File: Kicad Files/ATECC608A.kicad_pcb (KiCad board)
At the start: 2 copper layers, 26.7 x 22.8 mm, 12 parts, among them J1 Conn_01x04, U1 ATECC608A-SSHDA

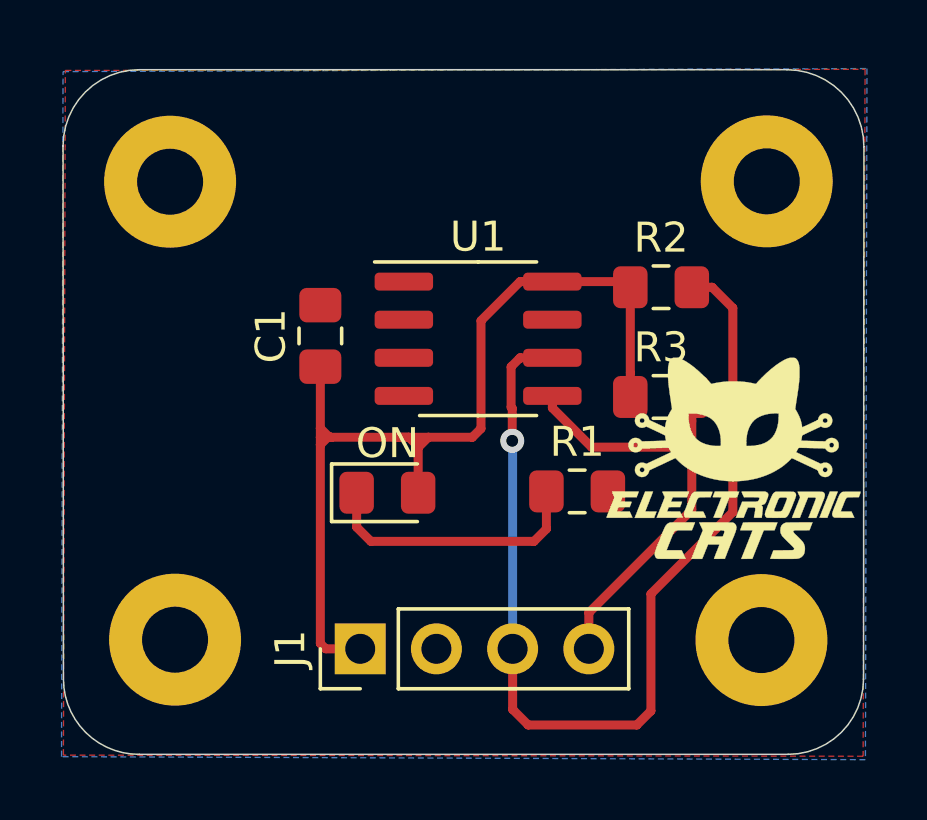
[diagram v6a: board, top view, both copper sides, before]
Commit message: add logos
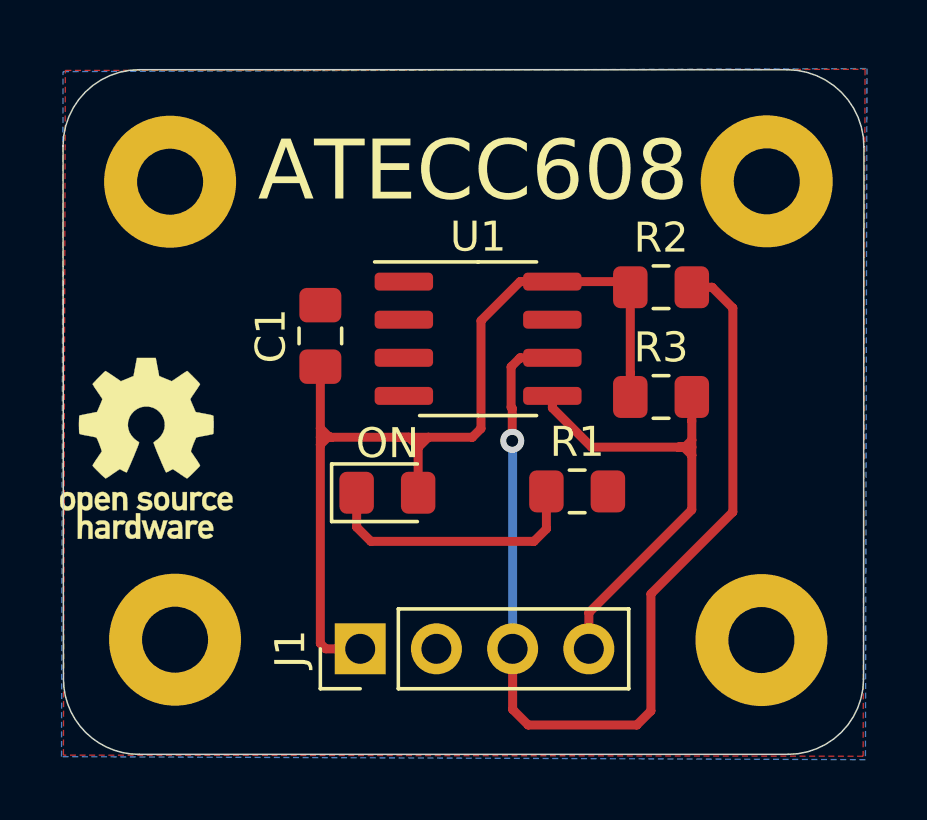
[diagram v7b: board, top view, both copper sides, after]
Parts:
- added REF**: OSHW-Logo_5.7x6mm_SilkScreen, Symbol:OSHW-Logo_5.7x6mm_SilkScreen, F.Cu at (153.9, 43.1)
- G***: moved to B.Cu
- moved G*** 12.4 mm to (164.8, 34.6), turned to 180 degrees
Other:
- board text added: "ATECC608"
- board text added: "ATECC608A"
- board text added: "Co-Proccesor"
- board text added: "Cryptographic"
- board text added: "v1.0"

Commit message: add pins logos
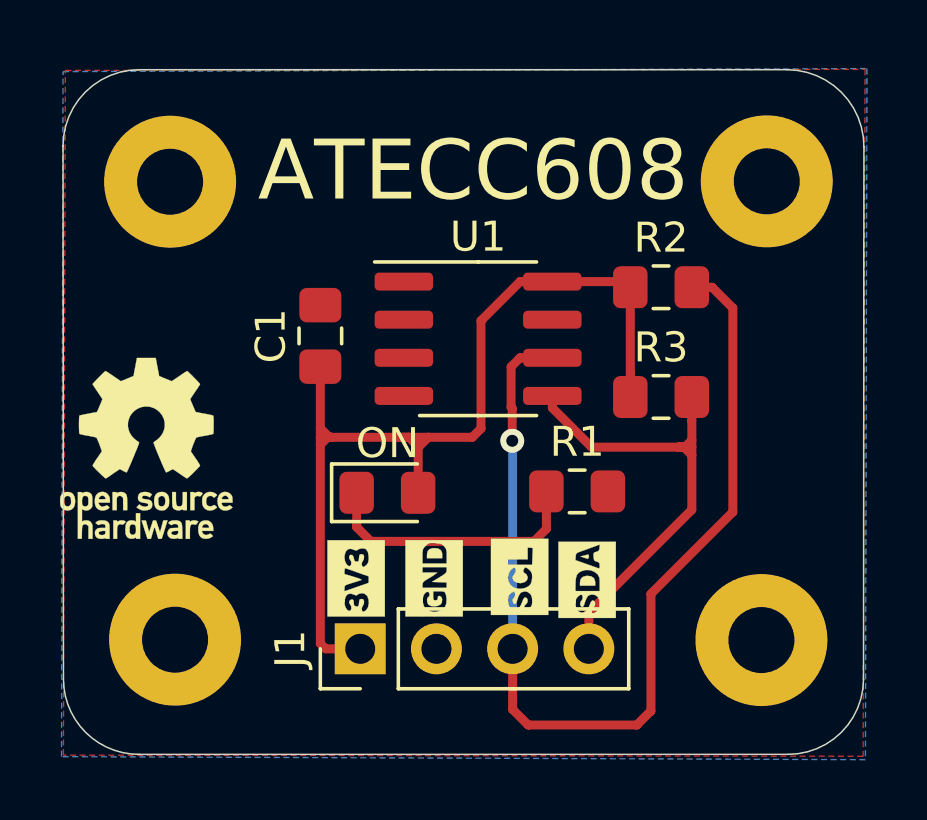
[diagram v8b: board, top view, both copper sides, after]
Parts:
- added G***: LOGO, GND, F.Cu at (163.5, 47.5)
- added G***: LOGO, 3v3, F.Cu at (160.9, 47.5)
- added G***: LOGO, SCL, F.Cu at (166.3, 47.4)
- added G***: LOGO, SDA, F.Cu at (168.6, 47.5)
